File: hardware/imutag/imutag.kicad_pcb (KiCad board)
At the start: 2 copper layers, 18 x 9 mm, 26 parts, among them J201 CONN_02X04, J301 Conn_01x01, J302 Conn_01x01, J303 Conn_01x01, J304 Conn_01x01, J401 CONN_01X02, Q501 Q_NPN_BEC, U1 at25ex321D-UUN, U2 AK09940A, U3 LPS22DF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

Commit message: checkpoint
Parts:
- C502, Q501: moved to B.Cu
- D401: moved to F.Cu
- J401: footprint AccelTag:MS621 -> AccelTag:batterypads
- moved Q501 4.76 mm to (152.6, 107.1)
- moved J301 2.45 mm to (154.0, 111.7)
- moved J302 2.45 mm to (154.0, 105.2)
- moved D401 2.41 mm to (154.8, 108.5), turned to 0 degrees
- moved C502 1.55 mm to (151.3, 111.0), turned to 90 degrees
- moved J401 0.80 mm to (156.2, 108.5), turned to -90 degrees
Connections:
- C7 pad 1: VBAT -> VIN
- D401 pad 1: VBAT -> VIN
- D401 pad 2: VIN -> VBAT
- U4 pad 3: VBAT -> VIN
- U4 pad 4: VBAT -> VIN
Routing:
- net GND: track 57.7 -> 77.0 mm, vias 5 -> 6
- net RST: track 9.86 -> 2.00 mm, vias 1 -> 0
- net VBAT: track 1.81 -> 7.16 mm, vias 0 -> 1
- net VIN: track 0.13 -> 5.46 mm, vias 0 -> 1
- net SWDIO: track 9.49 -> 14.1 mm
- net Net-(Q501-C): track 6.93 -> 11.0 mm, vias 1 -> 0
- net SWCLK: track 12.1 -> 10.2 mm
- net +1V8: track 38.9 -> 40.7 mm, vias 4 -> 6

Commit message: checkpoint
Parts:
- U2: moved to F.Cu
- U5: moved to B.Cu
- moved C8 10.3 mm to (152.6, 107.1), turned to 0 degrees
- moved C5 6.75 mm to (146.0, 108.5)
- moved C3 4.70 mm to (142.2, 108.5)
- moved U5 4.20 mm to (142.1, 108.5)
- moved U2 4.03 mm to (145.9, 110.1), turned to 180 degrees
- moved C1 3.13 mm to (142.2, 107.7), turned to 0 degrees
- moved C2 0.46 mm to (143.8, 105.8)
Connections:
- U2 pad A3: /AK_CK -> /AK_USART2_CK
- U2 pad A4: /AK_MOSI -> /AK_USART2_TX
- U2 pad B4: /AK_MISO -> /AK_USART2_RX
- U302 pad 10: /USART2_CK -> /AK_USART2_CK
- U302 pad 11: /AK_CK -> /LSM_CK
- U302 pad 12: /AK_MISO -> /LSM_MISO
- U302 pad 13: /AK_MOSI -> /LSM_MOSI
- U302 pad 15: /AK_CS -> /LSM_CS
- U302 pad 7: /ACCEL_CS -> /AK_CS
- U302 pad 8: /USART2_TX -> /AK_USART2_TX
- U302 pad 9: /USART2_RX -> /AK_USART2_RX
- U5 pad 1: /USART2_RX -> /LSM_MISO
- U5 pad 12: /ACCEL_CS -> /LSM_CS
- U5 pad 13: /USART2_CK -> /LSM_CK
- U5 pad 14: /USART2_TX -> /LSM_MOSI
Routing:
- net +1V8: track 40.7 -> 56.9 mm
- net /ACCEL_CS: track 8.38 -> 0.00 mm, vias 1 -> 0
- net /WKUP1: track 2.21 -> 7.53 mm, vias 1 -> 0
- net /AK_USART2_CK: track 0.00 -> 5.31 mm, vias 0 -> 1
- net /USART2_RX: track 3.36 -> 0.00 mm, vias 1 -> 0
- net /AK_CK: track 2.75 -> 0.00 mm
- net /LSM_MISO: track 0.00 -> 2.61 mm
- net /AK_MOSI: track 2.59 -> 0.00 mm
- net /LSM_CK: track 0.00 -> 2.35 mm, vias 0 -> 2
- net /USART2_CK: track 2.34 -> 0.00 mm, vias 1 -> 0
- net /AK_USART2_TX: track 0.00 -> 2.32 mm, vias 0 -> 1
- net /LSM_CS: track 0.00 -> 2.29 mm
- net /LSM_MOSI: track 0.00 -> 2.29 mm
- net /AK_MISO: track 2.23 -> 0.00 mm, vias 2 -> 0
- net GND: track 77.0 -> 74.9 mm
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
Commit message: checkpoint
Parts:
- moved J301 2.74 mm to (156.7, 112.1)
- moved J302 2.72 mm to (156.7, 104.9)
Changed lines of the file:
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@@
 			(pintype "passive")
 		)
+		(model "${KIPRJMOD}/lipo.step"
+			(offset
+				(xyz 0 -0.8 0.5)
+			)
+			(scale
+				(xyz 1 1 1)
+			)
+			(rotate
+				(xyz 90 0 -90)
+			)
+		)
 	)
 	(footprint "AccelTag:RV-8803-C7"
@@
 	(footprint "AccelTag:taghole1.1mm"
 		(layer "F.Cu")
-		(at 154 111.671)
+		(at 156.7 112.11)
 		(property "Reference" "J301"
 			(at 0 1.9812 0)
@@
 	(footprint "AccelTag:taghole1.1mm"
 		(layer "F.Cu")
-		(at 154 105.191)
+		(at 156.7 104.89)
 		(property "Reference" "J302"
 			(at 0 1.9812 0)
@@
 		(tags "capacitor")
 		(property "Reference" "C1"
-			(at 0 -1.05 360)
+			(at 0 -1.05 0)
 			(layer "F.SilkS")
 			(hide yes)
@@
 		)
 		(property "Value" "0.1uf"
-			(at 0 1.05 360)
+			(at 0 1.05 0)
 			(layer "F.Fab")
 			(hide yes)
@@
 		)
 		(property "Footprint" "Capacitor_SMD:C_0201_0603Metric"
-			(at 0 0 360)
+			(at 0 0 0)
 			(layer "F.Fab")
 			(hide yes)
@@
 		)
 		(property "Datasheet" ""
-			(at 0 0 360)
+			(at 0 0 0)
 			(layer "F.Fab")
 			(hide yes)
@@
 		)
 		(property "Description" ""
-			(at 0 0 360)
+			(at 0 0 0)
 			(layer "F.Fab")
 			(hide yes)
@@
 		)
 		(property "DISTPN" "490-10403-1-ND"
-			(at 0 0 360)
+			(at 0 0 0)
 			(layer "F.Fab")
 			(hide yes)
@@
 		)
 		(property "LCSC" "C181047"
-			(at 0 0 360)
+			(at 0 0 0)
 			(layer "F.Fab")
 			(hide yes)
@@
 		)
 		(property "MFN" "Murata"
-			(at 0 0 360)
+			(at 0 0 0)
 			(layer "F.Fab")
 			(hide yes)
@@
 		)
 		(property "MPN" "C181047"
-			(at 0 0 360)
+			(at 0 0 0)
 			(layer "F.Fab")
 			(hide yes)
@@
 		)
 		(property "Macrofab" ""
-			(at 0 0 360)
+			(at 0 0 0)
 			(layer "F.Fab")
 			(hide yes)
@@
 		)
 		(fp_text user "${REFERENCE}"
-			(at 0 -0.68 360)
+			(at 0 -0.68 0)
 			(layer "F.Fab")
 			(hide yes)
@@
 		(tags "capacitor")
 		(property "Reference" "C3"
-			(at 0 -1.05 360)
+			(at 0 -1.05 0)
 			(layer "F.SilkS")
 			(hide yes)
@@
 		)
 		(property "Value" "0.1uf"
-			(at 0 1.05 360)
+			(at 0 1.05 0)
 			(layer "F.Fab")
 			(hide yes)
@@
 		)
 		(fp_text user "${REFERENCE}"
-			(at 0 -0.68 360)
+			(at 0 -0.68 0)
 			(layer "F.Fab")
 			(effects
@@
 		(tags "LSM6DSV ")
 		(property "Reference" "U5"
-			(at 0 0 270)
+			(at 0 0 -90)
 			(unlocked yes)
 			(layer "B.SilkS")

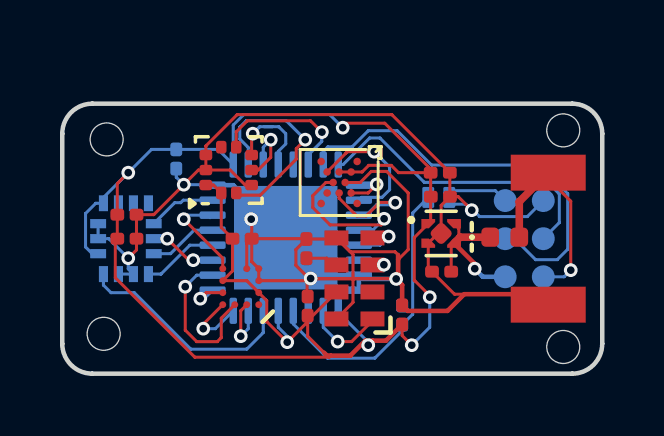
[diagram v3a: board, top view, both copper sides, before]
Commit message: complete IMU tag
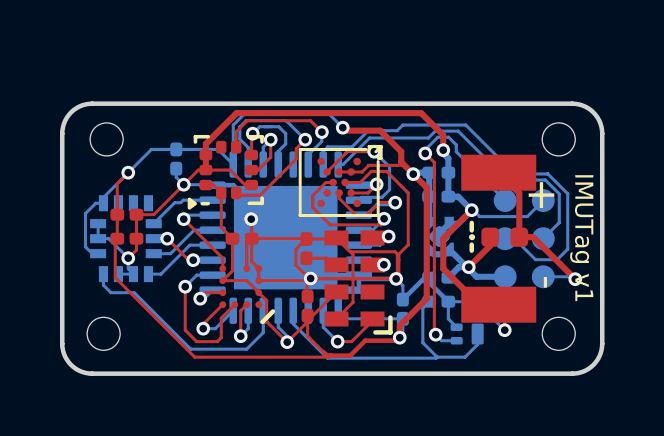
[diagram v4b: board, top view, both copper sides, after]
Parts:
- C501, C7, C8, C9, U4: moved to B.Cu
- moved Q501 4.65 mm to (153.5, 111.7), turned to 0 degrees
- moved J401 1.65 mm to (154.6, 108.5)
- moved C502 1.30 mm to (152.6, 110.6), turned to 0 degrees
- moved J301 0.46 mm to (156.6, 111.7)
- moved J302 0.34 mm to (156.6, 105.2)
- moved C7 0.22 mm to (152.6, 109.8)
- moved C501 0.19 mm to (151.4, 110.8)
- moved U4 0.12 mm to (152.6, 108.4), turned to -90 degrees
- moved C8 0.05 mm to (152.6, 107.1)
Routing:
- net RST: track 2.00 -> 11.0 mm, vias 0 -> 2
- net GND: track 74.9 -> 78.9 mm, vias 6 -> 8
- net VBAT: track 7.16 -> 6.02 mm
- net +1V8: track 56.9 -> 57.9 mm, vias 6 -> 5
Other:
- board text added: "+"
- board text added: "-"
- board text added: "IMUTag v1"

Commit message: update flash for imu tag
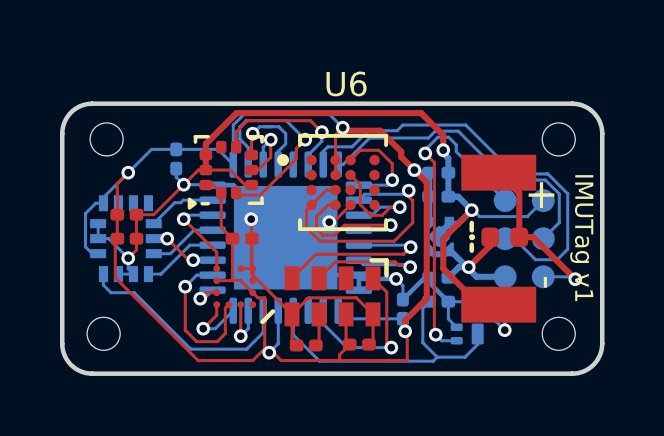
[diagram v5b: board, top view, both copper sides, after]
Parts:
- removed U1: at25ex321D-UUN, AccelTag:adesto_wlcsp12
- added U6: ~, AccelTag:IC_MX25U12843GBBI00, F.Cu at (149.4, 106.6)
- moved R1 3.23 mm to (148.1, 112.1), turned to 180 degrees
- moved C503 2.15 mm to (149.9, 112.0), turned to 0 degrees
- moved U501 0.94 mm to (149.0, 110.4), turned to -90 degrees
- moved U2 0.20 mm to (145.8, 110.1)
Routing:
- net GND: track 78.9 -> 63.8 mm
- net /SDA: track 1.67 -> 6.14 mm
- net /AT25_SCK: track 4.50 -> 8.82 mm
- net /SCL: track 1.28 -> 5.15 mm
- net /clkout: track 2.66 -> 5.59 mm
- net +1V8: track 57.9 -> 55.7 mm
- net /AT25_nCS: track 1.66 -> 3.44 mm

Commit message: added nucleoshield template
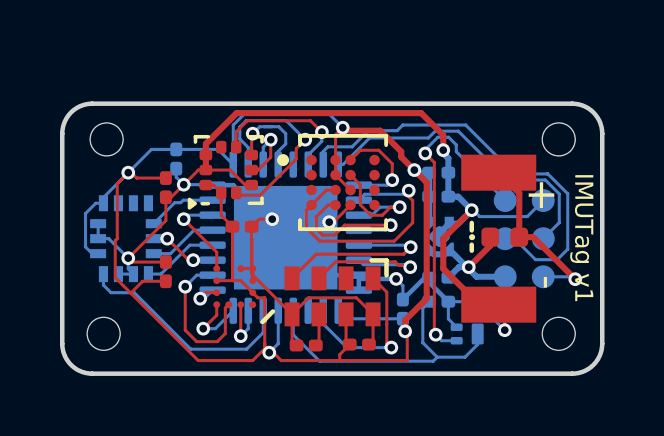
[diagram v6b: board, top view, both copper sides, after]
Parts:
- moved C3 1.70 mm to (143.5, 109.6), turned to 90 degrees
- moved C1 1.58 mm to (143.5, 106.8), turned to -90 degrees
- moved C5 0.40 mm to (146.0, 108.1)
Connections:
- U6 pad C3: unconnected-(U6-~{WP}-PadC3) -> +1V8
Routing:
- net +1V8: track 55.7 -> 58.9 mm
- net GND: track 63.8 -> 65.2 mm

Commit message: imu tag breakout
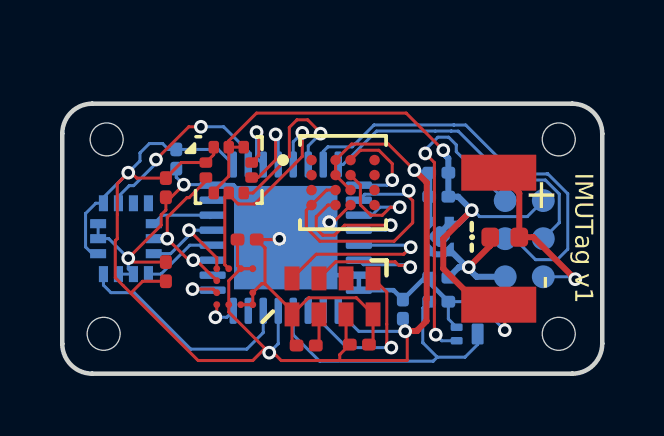
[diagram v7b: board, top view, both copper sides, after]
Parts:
- moved C5 0.46 mm to (146.2, 108.5)
- turned U2 to 90 degrees
- turned U3 to 0 degrees
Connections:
- U2 pad A1: unconnected-(U2-DRDY/TRG-PadA1) -> /AK_TRG
- U2 pad A3: /AK_USART2_CK -> /LSM_CK
- U2 pad A4: /AK_USART2_TX -> /LSM_MOSI
- U2 pad B4: /AK_USART2_RX -> /LPS_MISO
- U2 pad D4: /AK_RSTN -> +1V8
- U3 pad 2: /USART1_CK -> /LSM_CK
- U3 pad 4: /USART1_TX -> /LPS_MISO
- U3 pad 5: /USART1_RX -> /LPS_MOSI
- U3 pad 7: unconnected-(U3-INT_DRDY-Pad7) -> /LPS_DRDY
- U302 pad 10: /AK_USART2_CK -> unconnected-(U302-PA4-Pad10)
- U302 pad 14: /AK_RSTN -> /LSM_CS
- U302 pad 15: /LSM_CS -> unconnected-(U302-PB1-Pad15)
- U302 pad 18: /USART1_CK -> /LSM_TRG
- U302 pad 19: /USART1_TX -> /LPS_DRDY
- U302 pad 20: /USART1_RX -> /LPS_CS
- U302 pad 21: unconnected-(U302-PA11-Pad21) -> /LPS_MISO
- U302 pad 22: /LPS_CS -> /LPS_MOSI
- U302 pad 7: /AK_CS -> unconnected-(U302-PA1-Pad7)
- U302 pad 8: /AK_USART2_TX -> /AK_TRG
- U302 pad 9: /AK_USART2_RX -> /AK_CS
- U5 pad 9: unconnected-(U5-INT2-Pad9) -> /LSM_TRG
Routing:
- net /LPS_MISO: track 0.00 -> 7.92 mm, vias 0 -> 1
- net /USART1_CK: track 7.20 -> 0.00 mm, vias 1 -> 0
- net /LSM_TRG: track 0.00 -> 6.37 mm, vias 0 -> 2
- net GND: track 65.2 -> 59.0 mm, vias 8 -> 7
- net +1V8: track 58.9 -> 53.0 mm, vias 5 -> 4
- net /LPS_MOSI: track 0.00 -> 5.69 mm, vias 0 -> 1
- net /AK_USART2_CK: track 5.22 -> 0.00 mm, vias 1 -> 0
- net /LSM_CK: track 2.35 -> 6.03 mm
- net /USART1_RX: track 3.42 -> 0.00 mm, vias 1 -> 0
- net /AK_RSTN: track 3.24 -> 0.00 mm, vias 1 -> 0
- net /AK_USART2_TX: track 2.38 -> 0.00 mm, vias 1 -> 0
- net /USART1_TX: track 2.33 -> 0.00 mm, vias 1 -> 0
- net /LPS_DRDY: track 0.00 -> 2.32 mm, vias 0 -> 1
- net /LPS_CS: track 4.95 -> 2.95 mm
- net /LSM_MOSI: track 2.29 -> 4.07 mm, vias 0 -> 1
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
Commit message: checkpoint
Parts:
- moved C503 2.72 mm to (147.4, 111.1), turned to -90 degrees
- moved R1 2.62 mm to (147.3, 109.6), turned to 90 degrees
- moved C501 0.72 mm to (151.1, 111.5)
- moved U501 0.07 mm to (149.0, 110.5), turned to 180 degrees
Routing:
- net /SDA: track 6.14 -> 3.94 mm
- net /clkout: track 5.59 -> 3.66 mm
- net GND: track 59.0 -> 60.5 mm
- net /SCL: track 5.15 -> 4.20 mm
